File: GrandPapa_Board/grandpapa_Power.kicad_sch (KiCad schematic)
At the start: 34 parts, among them U1 MCP1642B-50I/MS, U2 BD9E302EFJ, U5 FPF2124, U6 INA180

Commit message: Add footprints, inductors TBD
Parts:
- C1, C13, C15, C2, C3, C4, C5, C6, C7, C8: footprint (none) -> Capacitor_SMD:C_0805_2012Metric_Pad1.18x1.45mm_HandSolder
- F1, F2: footprint (none) -> Fuse:Fuse_0805_2012Metric_Pad1.15x1.40mm_HandSolder
- R10, R16, R19, R2, R25, R3, R9: footprint (none) -> Resistor_SMD:R_0805_2012Metric_Pad1.20x1.40mm_HandSolder
- R27, R7, R8: footprint Resistor_SMD:R_1206_3216Metric_Pad1.30x1.75mm_HandSolder -> Resistor_SMD:R_0805_2012Metric_Pad1.20x1.40mm_HandSolder
- TP3: footprint (none) -> Connector_PinHeader_2.54mm:PinHeader_1x01_P2.54mm_Vertical
- U1: footprint (none) -> Package_SO:MSOP-8_3x3mm_P0.65mm
- U2: footprint (none) -> Package_SO:HTSOP-8-1EP_3.9x4.9mm_P1.27mm_EP2.4x3.2mm
- U5, U6: footprint (none) -> Package_TO_SOT_SMD:SOT-23-5_HandSoldering
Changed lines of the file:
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@@
     (property "Reference" "U5" (id 0) (at 186.055 120.65 0))
     (property "Value" "FPF2124" (id 1) (at 186.055 122.555 0))
-    (property "Footprint" "" (id 2) (at 186.055 128.905 0)
+    (property "Footprint" "Package_TO_SOT_SMD:SOT-23-5_HandSoldering" (id 2) (at 186.055 128.905 0)
       (effects (font (size 1.27 1.27)) hide)
     )
@@
     (property "Reference" "R7" (id 0) (at 196.977 134.112 0))
     (property "Value" "500R" (id 1) (at 196.469 135.89 0))
-    (property "Footprint" "Resistor_SMD:R_1206_3216Metric_Pad1.30x1.75mm_HandSolder" (id 2) (at 201.041 136.144 90)
+    (property "Footprint" "Resistor_SMD:R_0805_2012Metric_Pad1.20x1.40mm_HandSolder" (id 2) (at 201.041 136.144 90)
       (effects (font (size 1.27 1.27)) hide)
     )
@@
     (property "Reference" "U6" (id 0) (at 86.36 69.215 0))
     (property "Value" "INA180" (id 1) (at 86.36 71.755 0))
-    (property "Footprint" "" (id 2) (at 87.63 59.69 0)
+    (property "Footprint" "Package_TO_SOT_SMD:SOT-23-5_HandSoldering" (id 2) (at 87.63 59.69 0)
       (effects (font (size 1.27 1.27)) hide)
     )
@@
     (property "Reference" "R25" (id 0) (at 238.125 52.705 90))
     (property "Value" "324kR" (id 1) (at 238.125 54.483 90))
-    (property "Footprint" "" (id 2) (at 238.125 56.515 0)
+    (property "Footprint" "Resistor_SMD:R_0805_2012Metric_Pad1.20x1.40mm_HandSolder" (id 2) (at 238.125 56.515 0)
       (effects (font (size 1.27 1.27)) hide)
     )
@@
       (effects (font (size 1.27 1.27)) (justify left))
     )
-    (property "Footprint" "" (id 2) (at 191.77 40.005 0)
+    (property "Footprint" "Capacitor_SMD:C_0805_2012Metric_Pad1.18x1.45mm_HandSolder" (id 2) (at 191.77 40.005 0)
       (effects (font (size 1.27 1.27)) hide)
     )
@@
       (effects (font (size 1.27 1.27)) (justify left))
     )
-    (property "Footprint" "" (id 2) (at 165.1 130.81 0)
+    (property "Footprint" "Capacitor_SMD:C_0805_2012Metric_Pad1.18x1.45mm_HandSolder" (id 2) (at 165.1 130.81 0)
       (effects (font (size 1.27 1.27)) hide)
     )
@@
       (effects (font (size 1.27 1.27)) (justify left))
     )
-    (property "Footprint" "" (id 2) (at 209.55 130.81 0)
+    (property "Footprint" "Capacitor_SMD:C_0805_2012Metric_Pad1.18x1.45mm_HandSolder" (id 2) (at 209.55 130.81 0)
       (effects (font (size 1.27 1.27)) hide)
     )
@@
       (effects (font (size 1.27 1.27)) (justify left))
     )
-    (property "Footprint" "" (id 2) (at 205.105 56.515 0)
+    (property "Footprint" "Capacitor_SMD:C_0805_2012Metric_Pad1.18x1.45mm_HandSolder" (id 2) (at 205.105 56.515 0)
       (effects (font (size 1.27 1.27)) hide)
     )
@@
     (property "Reference" "R3" (id 0) (at 128.27 168.275 0))
     (property "Value" "100R" (id 1) (at 128.27 170.18 0))
-    (property "Footprint" "" (id 2) (at 132.08 168.91 0)
+    (property "Footprint" "Resistor_SMD:R_0805_2012Metric_Pad1.20x1.40mm_HandSolder" (id 2) (at 132.08 168.91 0)
       (effects (font (size 1.27 1.27)) hide)
     )
@@
       (effects (font (size 1.27 1.27)) (justify left))
     )
-    (property "Footprint" "" (id 2) (at 179.705 40.005 0)
+    (property "Footprint" "Capacitor_SMD:C_0805_2012Metric_Pad1.18x1.45mm_HandSolder" (id 2) (at 179.705 40.005 0)
       (effects (font (size 1.27 1.27)) hide)
     )
@@
       (effects (font (size 1.27 1.27)) (justify left))
     )
-    (property "Footprint" "" (id 2) (at 125.73 130.81 0)
+    (property "Footprint" "Capacitor_SMD:C_0805_2012Metric_Pad1.18x1.45mm_HandSolder" (id 2) (at 125.73 130.81 0)
       (effects (font (size 1.27 1.27)) hide)
     )
@@
       (effects (font (size 1.27 1.27)) (justify left))
     )
-    (property "Footprint" "" (id 2) (at 159.385 125.73 0)
+    (property "Footprint" "Connector_PinHeader_2.54mm:PinHeader_1x01_P2.54mm_Vertical" (id 2) (at 159.385 125.73 0)
       (effects (font (size 1.27 1.27)) hide)
     )
@@
     (property "Reference" "F2" (id 0) (at 58.42 122.047 90))
     (property "Value" "1.2A" (id 1) (at 58.42 123.825 90))
-    (property "Footprint" "" (id 2) (at 63.5 125.095 0)
+    (property "Footprint" "Fuse:Fuse_0805_2012Metric_Pad1.15x1.40mm_HandSolder" (id 2) (at 63.5 125.095 0)
       (effects (font (size 1.27 1.27)) (justify left) hide)
     )
@@
     (property "Reference" "R27" (id 0) (at 158.115 43.815 0))
     (property "Value" "15k" (id 1) (at 158.115 46.355 0))
-    (property "Footprint" "Resistor_SMD:R_1206_3216Metric_Pad1.30x1.75mm_HandSolder" (id 2) (at 163.576 45.339 90)
+    (property "Footprint" "Resistor_SMD:R_0805_2012Metric_Pad1.20x1.40mm_HandSolder" (id 2) (at 163.576 45.339 90)
       (effects (font (size 1.27 1.27)) hide)
     )
@@
       (effects (font (size 1.27 1.27)) (justify left))
     )
-    (property "Footprint" "" (id 2) (at 66.04 130.175 0)
+    (property "Footprint" "Capacitor_SMD:C_0805_2012Metric_Pad1.18x1.45mm_HandSolder" (id 2) (at 66.04 130.175 0)
       (effects (font (size 1.27 1.27)) hide)
     )
@@
       (effects (font (size 1.27 1.27)) (justify left))
     )
-    (property "Footprint" "" (id 2) (at 88.265 121.285 0)
+    (property "Footprint" "Package_SO:MSOP-8_3x3mm_P0.65mm" (id 2) (at 88.265 121.285 0)
       (effects (font (size 1.27 1.27)) hide)
     )
@@
     (property "Reference" "R10" (id 0) (at 146.05 122.809 90))
     (property "Value" "0" (id 1) (at 146.05 124.333 90))
-    (property "Footprint" "" (id 2) (at 146.05 126.365 0)
+    (property "Footprint" "Resistor_SMD:R_0805_2012Metric_Pad1.20x1.40mm_HandSolder" (id 2) (at 146.05 126.365 0)
       (effects (font (size 1.27 1.27)) hide)
     )
@@
       (effects (font (size 1.27 1.27)) (justify left))
     )
-    (property "Footprint" "" (id 2) (at 238.125 68.58 0)
+    (property "Footprint" "Capacitor_SMD:C_0805_2012Metric_Pad1.18x1.45mm_HandSolder" (id 2) (at 238.125 68.58 0)
       (effects (font (size 1.27 1.27)) hide)
     )
@@
     (property "Reference" "F1" (id 0) (at 49.53 30.48 90))
     (property "Value" "1.2A" (id 1) (at 49.53 32.385 90))
-    (property "Footprint" "" (id 2) (at 54.61 34.29 0)
+    (property "Footprint" "Fuse:Fuse_0805_2012Metric_Pad1.15x1.40mm_HandSolder" (id 2) (at 54.61 34.29 0)
       (effects (font (size 1.27 1.27)) (justify left) hide)
     )
@@
     (property "Reference" "U2" (id 0) (at 213.995 27.94 0))
     (property "Value" "BD9E302EFJ" (id 1) (at 213.995 30.48 0))
-    (property "Footprint" "" (id 2) (at 213.995 31.75 0)
+    (property "Footprint" "Package_SO:HTSOP-8-1EP_3.9x4.9mm_P1.27mm_EP2.4x3.2mm" (id 2) (at 213.995 31.75 0)
       (effects (font (size 1.27 1.27)) hide)
     )
@@
     (property "Reference" "R2" (id 0) (at 115.57 130.175 90))
     (property "Value" "1MR" (id 1) (at 115.57 132.08 90))
-    (property "Footprint" "" (id 2) (at 115.57 133.985 0)
+    (property "Footprint" "Resistor_SMD:R_0805_2012Metric_Pad1.20x1.40mm_HandSolder" (id 2) (at 115.57 133.985 0)
       (effects (font (size 1.27 1.27)) hide)
     )
@@
     (property "Reference" "R9" (id 0) (at 90.17 32.004 90))
     (property "Value" "0" (id 1) (at 90.17 33.528 90))
-    (property "Footprint" "" (id 2) (at 90.17 35.56 0)
+    (property "Footprint" "Resistor_SMD:R_0805_2012Metric_Pad1.20x1.40mm_HandSolder" (id 2) (at 90.17 35.56 0)
       (effects (font (size 1.27 1.27)) hide)
     )
@@
       (effects (font (size 1.27 1.27)) (justify right))
     )
-    (property "Footprint" "" (id 2) (at 222.885 62.23 0)
+    (property "Footprint" "Resistor_SMD:R_0805_2012Metric_Pad1.20x1.40mm_HandSolder" (id 2) (at 222.885 62.23 0)
       (effects (font (size 1.27 1.27)) hide)
     )
@@
       (effects (font (size 1.27 1.27)) (justify right))
     )
-    (property "Footprint" "" (id 2) (at 205.105 62.865 0)
+    (property "Footprint" "Resistor_SMD:R_0805_2012Metric_Pad1.20x1.40mm_HandSolder" (id 2) (at 205.105 62.865 0)
       (effects (font (size 1.27 1.27)) hide)
     )
@@
     (property "Reference" "R8" (id 0) (at 159.385 53.975 0))
     (property "Value" "10k" (id 1) (at 159.385 56.515 0))
-    (property "Footprint" "Resistor_SMD:R_1206_3216Metric_Pad1.30x1.75mm_HandSolder" (id 2) (at 164.846 55.499 90)
+    (property "Footprint" "Resistor_SMD:R_0805_2012Metric_Pad1.20x1.40mm_HandSolder" (id 2) (at 164.846 55.499 90)
       (effects (font (size 1.27 1.27)) hide)
     )
@@
       (effects (font (size 1.27 1.27)) (justify left))
     )
-    (property "Footprint" "" (id 2) (at 257.175 62.23 0)
+    (property "Footprint" "Capacitor_SMD:C_0805_2012Metric_Pad1.18x1.45mm_HandSolder" (id 2) (at 257.175 62.23 0)
       (effects (font (size 1.27 1.27)) hide)
     )
@@
       (effects (font (size 1.27 1.27)) (justify left))
     )
-    (property "Footprint" "" (id 2) (at 234.95 35.56 0)
-      (effects (font (size 1.27 1.27)) hide)
-    )
+    (property "Footprint" "Capacitor_SMD:C_0805_2012Metric_Pad1.18x1.45mm_HandSolder" (id 2) (at 234.95 35.56 0)
+      (effects (font (size 1.27 1.27)) hide)
+    )

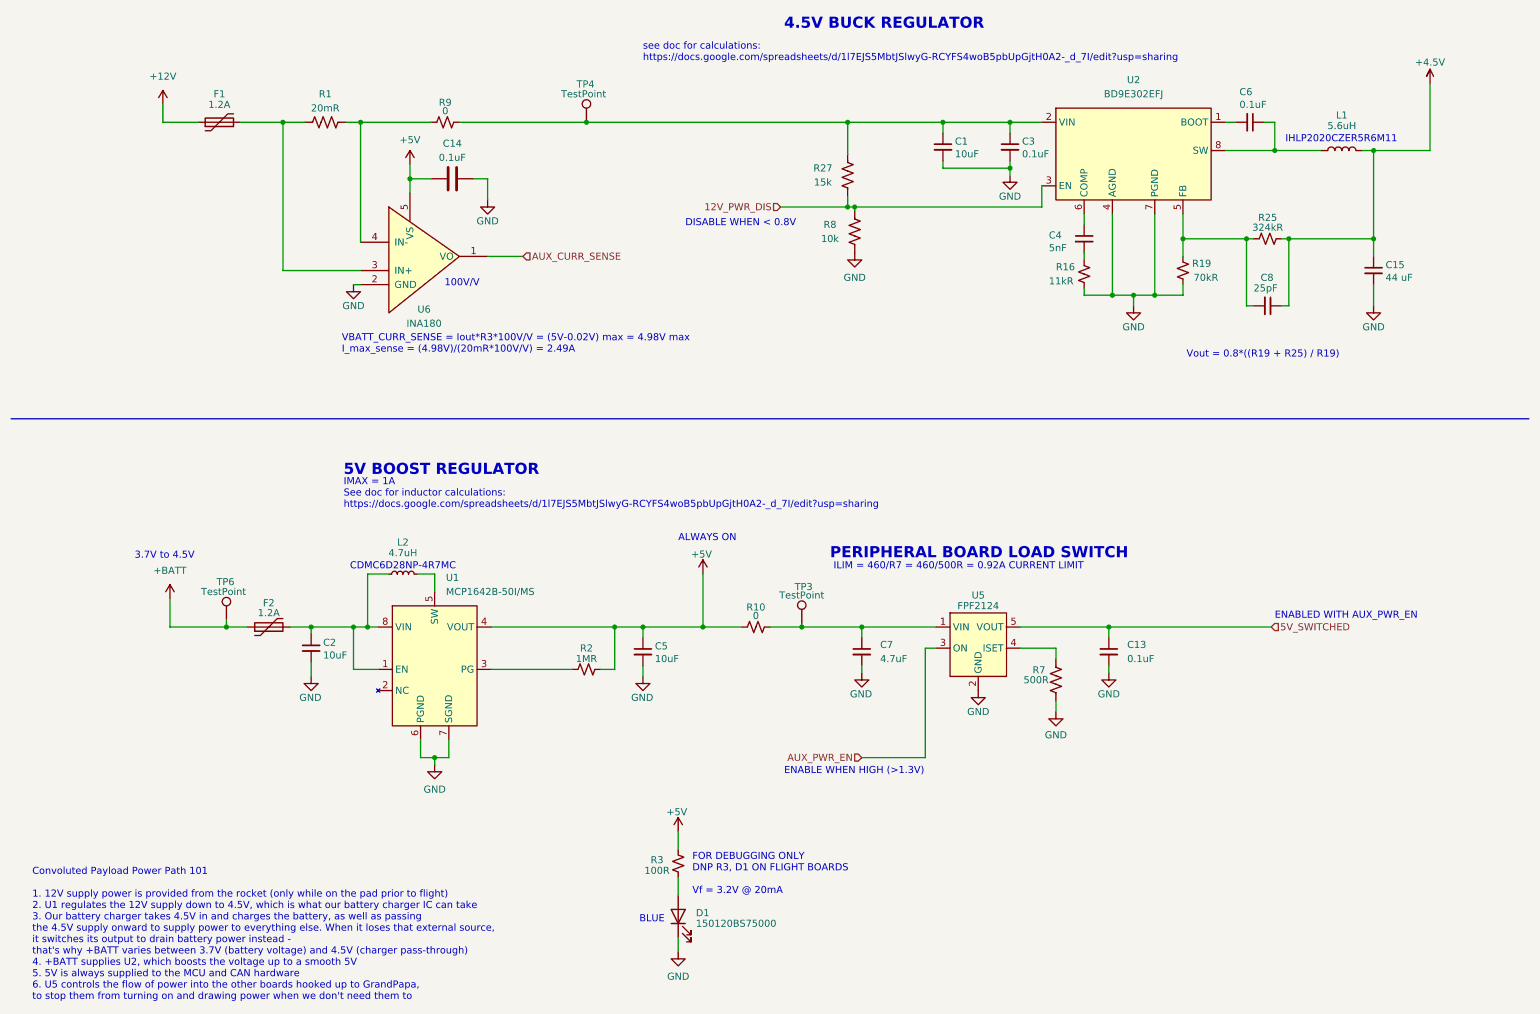
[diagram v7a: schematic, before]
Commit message: Finish footprints, add board outline
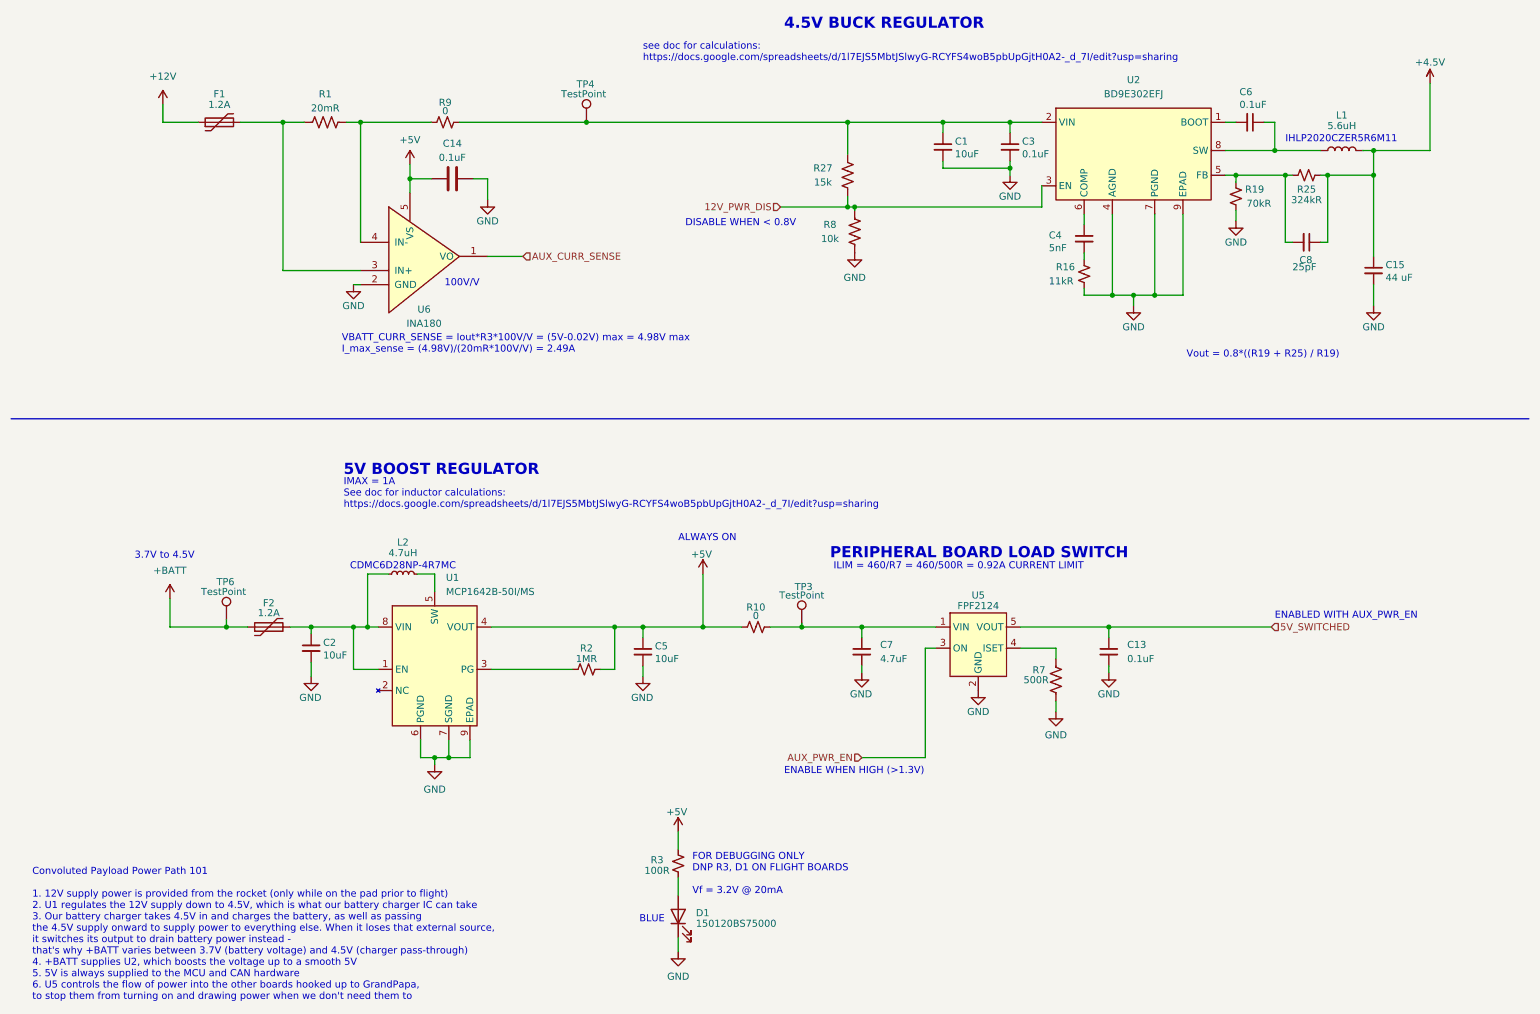
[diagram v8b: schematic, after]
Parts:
- L1: footprint (none) -> Inductor_SMD:L_Vishay_IHLP-2020
- L2: footprint (none) -> Inductor_SMD:L_Sumida_CDMC6D28_7.25x6.5mm
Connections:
- net GND: now also U1.9 (EPAD), U2.9 (EPAD)
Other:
- moved on the sheet: C8, R19, R25
